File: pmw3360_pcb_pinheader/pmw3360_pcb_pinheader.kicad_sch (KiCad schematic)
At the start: 20 parts, among them J1 Conn_01x08, U1 PMW3360DM-T2QU, U2 TPS73601DBV

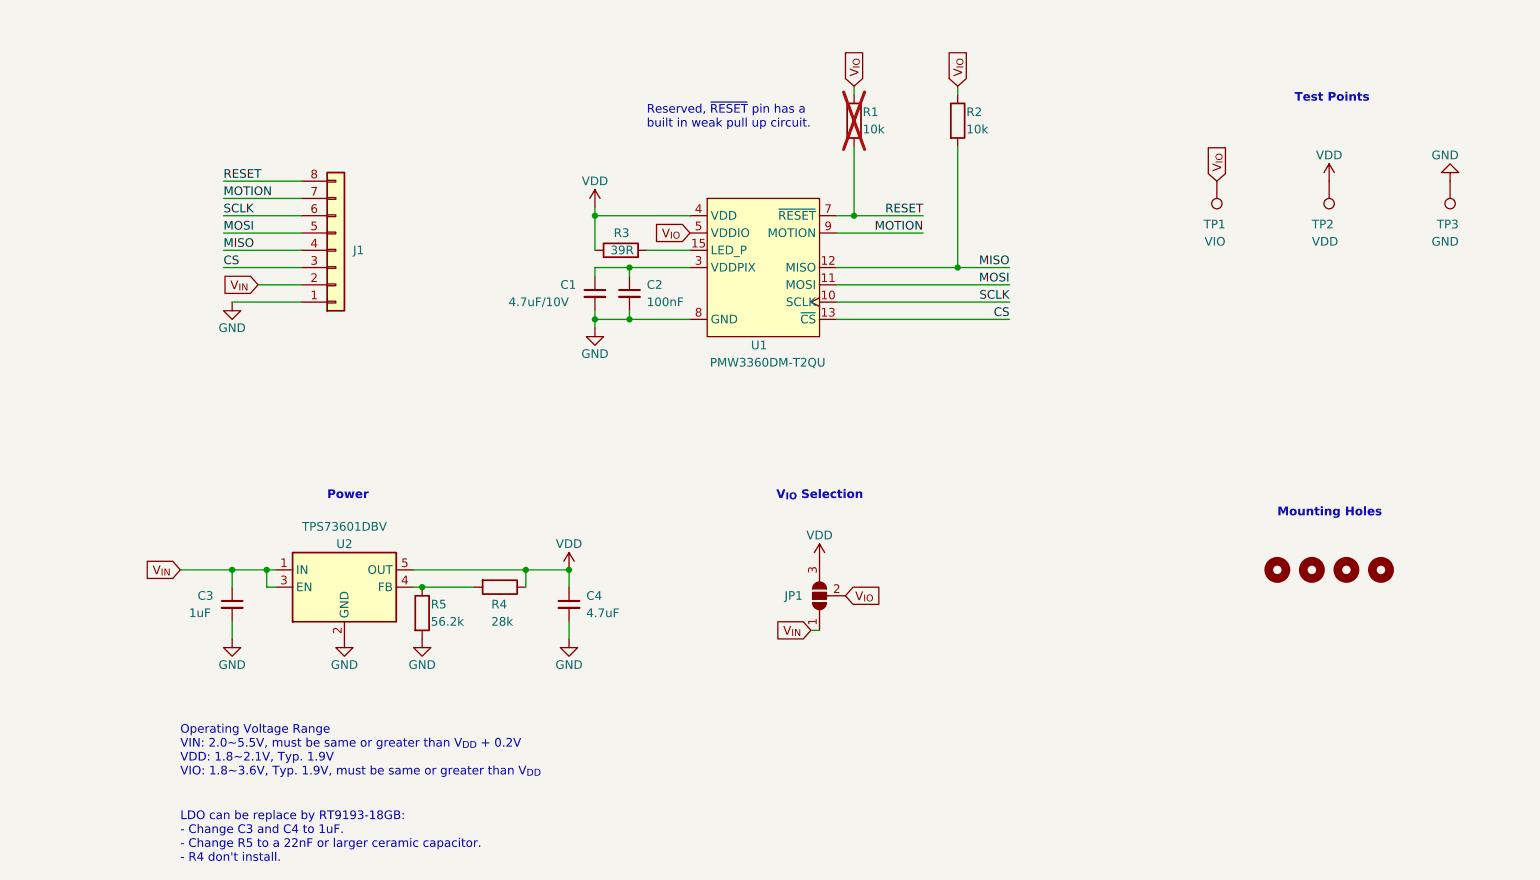
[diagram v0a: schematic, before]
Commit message: Change pin header edition LDO to TLV74318PDBVR
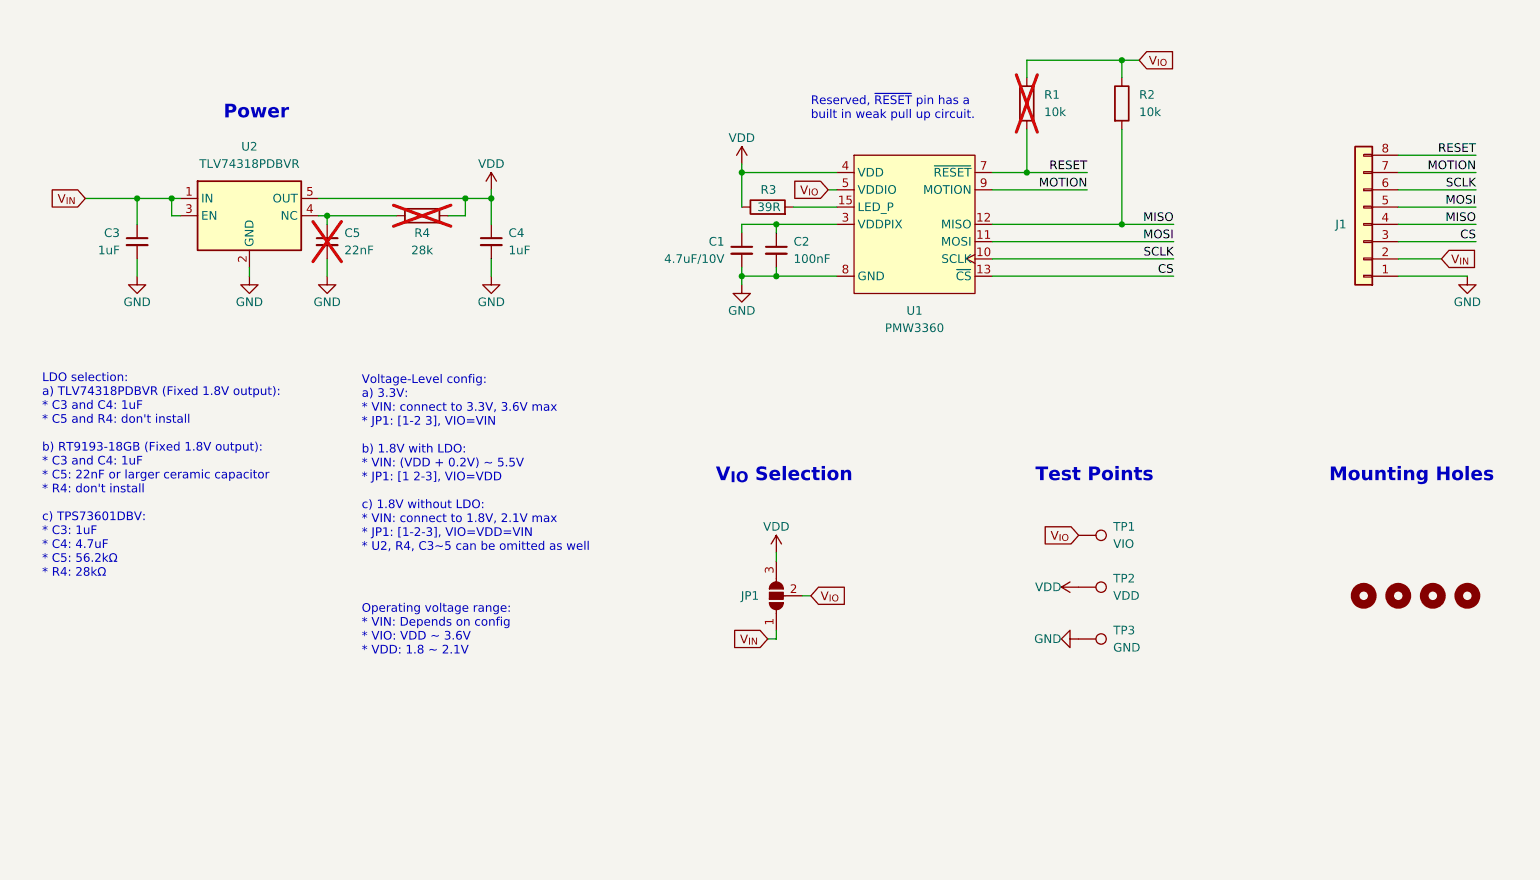
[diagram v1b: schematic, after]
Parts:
- removed R5: 56.2k, Resistor_SMD:R_0603_1608Metric_Pad0.98x0.95mm_HandSolder, symbol Device:R
- removed U2: TPS73601DBV, Package_TO_SOT_SMD:SOT-23-5, symbol Regulator_Linear:TPS73601DBV
- added C5: 22nF, Capacitor_SMD:C_0603_1608Metric_Pad1.08x0.95mm_HandSolder, symbol Device:C_Small
- added U2: TLV74318PDBVR, Package_TO_SOT_SMD:SOT-23-5, symbol PMW3360_PCB:TLV74318PDBVR
- C1: LCSC (none) -> C19666; Mfr. # (none) -> CL10A475KO8NNNC
- C2: LCSC (none) -> C14663; Mfr. # (none) -> CC0603KRX7R9BB104
- C3: LCSC (none) -> C15849; Mfr. # (none) -> CL10A105KB8NNNC
- C4: value 4.7uF -> 1uF; LCSC (none) -> C15849; Mfr. # (none) -> CL10A105KB8NNNC
- H1, H2, H3, H4, JP1, TP1, TP2, TP3: now left out of the parts list
- R1, R2: LCSC (none) -> C25804; Mfr. # (none) -> 0603WAF1002T5E
- R3: LCSC (none) -> C23154; Mfr. # (none) -> 0603WAF390JT5E
- R4: now not fitted
- U1: value PMW3360DM-T2QU -> PMW3360; footprint PMW3360_PCB:PMW3360DM-T2QU 16Pin -> PMW3360_PCB:16pin‐DIP(PMW3360DM-T2QU); Mfr. # (none) -> PMW3360DM-T2QU + LM19-LSI
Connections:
- net GND: now also C5.2, U2.2 (GND)
- net VDD: now also U2.5 (OUT)
- net V_{IN}: now also U2.1 (IN), U2.3 (EN)
- net at R4.2: now also C5.1, U2.4 (NC)
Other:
- note added: "LDO selection: a) TLV74318PDBVR (Fixed 1.8V output): * C3 and C4: 1uF * C5 and R4: don't install b) RT9193-18GB (Fixed 1.8V output): * C3 and C4: 1uF * C5: 22nF or larger ceramic capacitor * R4: don't install c) TPS73601DBV: * C3: 1uF * C4: 4.7uF * C5: 56.2kΩ * R4: 28kΩ"
- note added: "Operating voltage range: * VIN: Depends on config * VIO: VDD ~ 3.6V * VDD: 1.8 ~ 2.1V"
- note added: "Voltage-Level config: a) 3.3V: * VIN: connect to 3.3V, 3.6V max * JP1: [1-2 3], VIO=VIN b) 1.8V with LDO: * VIN: (VDD + 0.2V) ~ 5.5V * JP1: [1 2-3], VIO=VDD c) 1.8V without LDO: * VIN: connect to 1.8V, 2.1V max * JP1: [1-2-3], VIO=VDD=VIN * U2, R4, C3~5 can be omitted as well"
- note removed: "LDO can be replace by RT9193-18GB: - Change C3 and C4 to 1uF. - Change R5 to a 22nF or larger ceramic capacitor. - R4 don't install."
- note removed: "Operating Voltage Range VIN: 2.0~5.5V, must be same or greater than V_{DD} + 0.2V VDD: 1.8~2.1V, Typ. 1.9V VIO: 1.8~3.6V, Typ. 1.9V, must be same or greater than V_{DD}"
- moved on the sheet: C1, C2, C3, J1, JP1, R1, R2, R3, TP1, TP2, TP3, U1
